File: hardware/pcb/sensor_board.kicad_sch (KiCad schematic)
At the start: 43 parts, among them J1 12V_INN, J10 CHT2 Termopar, J11 CHT3 Termopar, J12 CHT4 Termopar, J15 GPS NEO-6M, J2 Olje Temp NTC, J3 IAT Inntaksluft NTC, J4 Olje Trykk 0-10bar, J5 Lambda Innovate LC-2, J6 Batteri 12-15V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

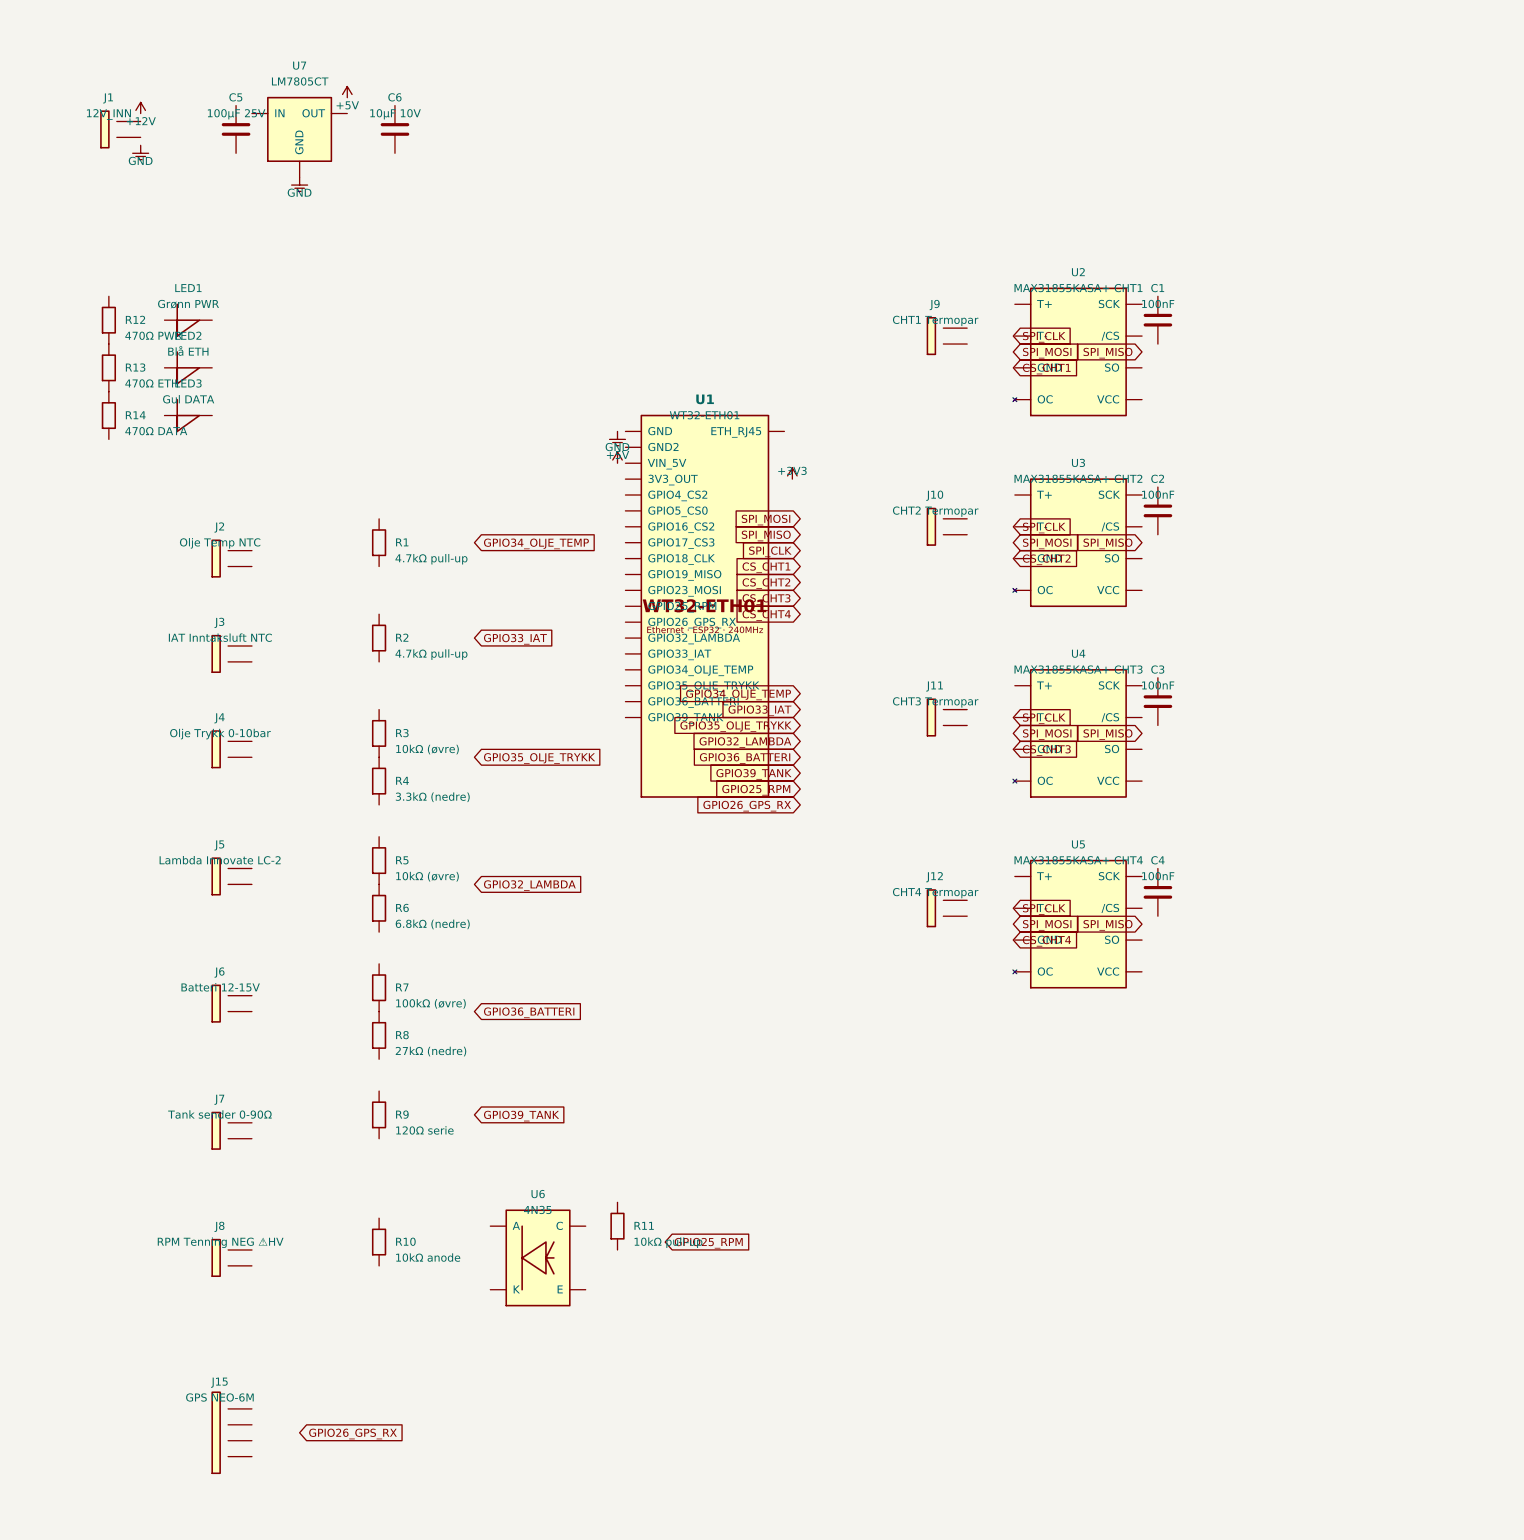
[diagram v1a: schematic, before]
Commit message: Sensorkortet v2: GPIO-fix, EGT1, vifte-MOSFET, GPS fjernet
- Rettede GPIO-pinner (ETH-konflikt): SCK=GPIO14, MISO=GPIO12
  CS: CHT1=GPIO5, CHT2=GPIO13, CHT3=GPIO15, CHT4=GPIO17
  RPM=GPIO4, EGT1=GPIO16, FAN=GPIO2
- Lagt til U8 (MAX31855 for EGT1 eksostemperatur)
- Lagt til Q1 (IRLB8721 MOSFET) for 12V viftestyring
- Lagt til D1 (1N4007 flyback-diode) for motorbeskyttelse
- Lagt til R15 (100R gate), R16 (10k pull-down), J17 (vifte-klemme)
- Fjernet GPS-header (NEO-6M kobles direkte til RPi via USB)
- 291 gyldige UUIDs, 0 duplikater, 0 ugyldige pin-shapes

https://claude.ai/code/session_01NVvsy3kMr9piDWfs5WdvpG
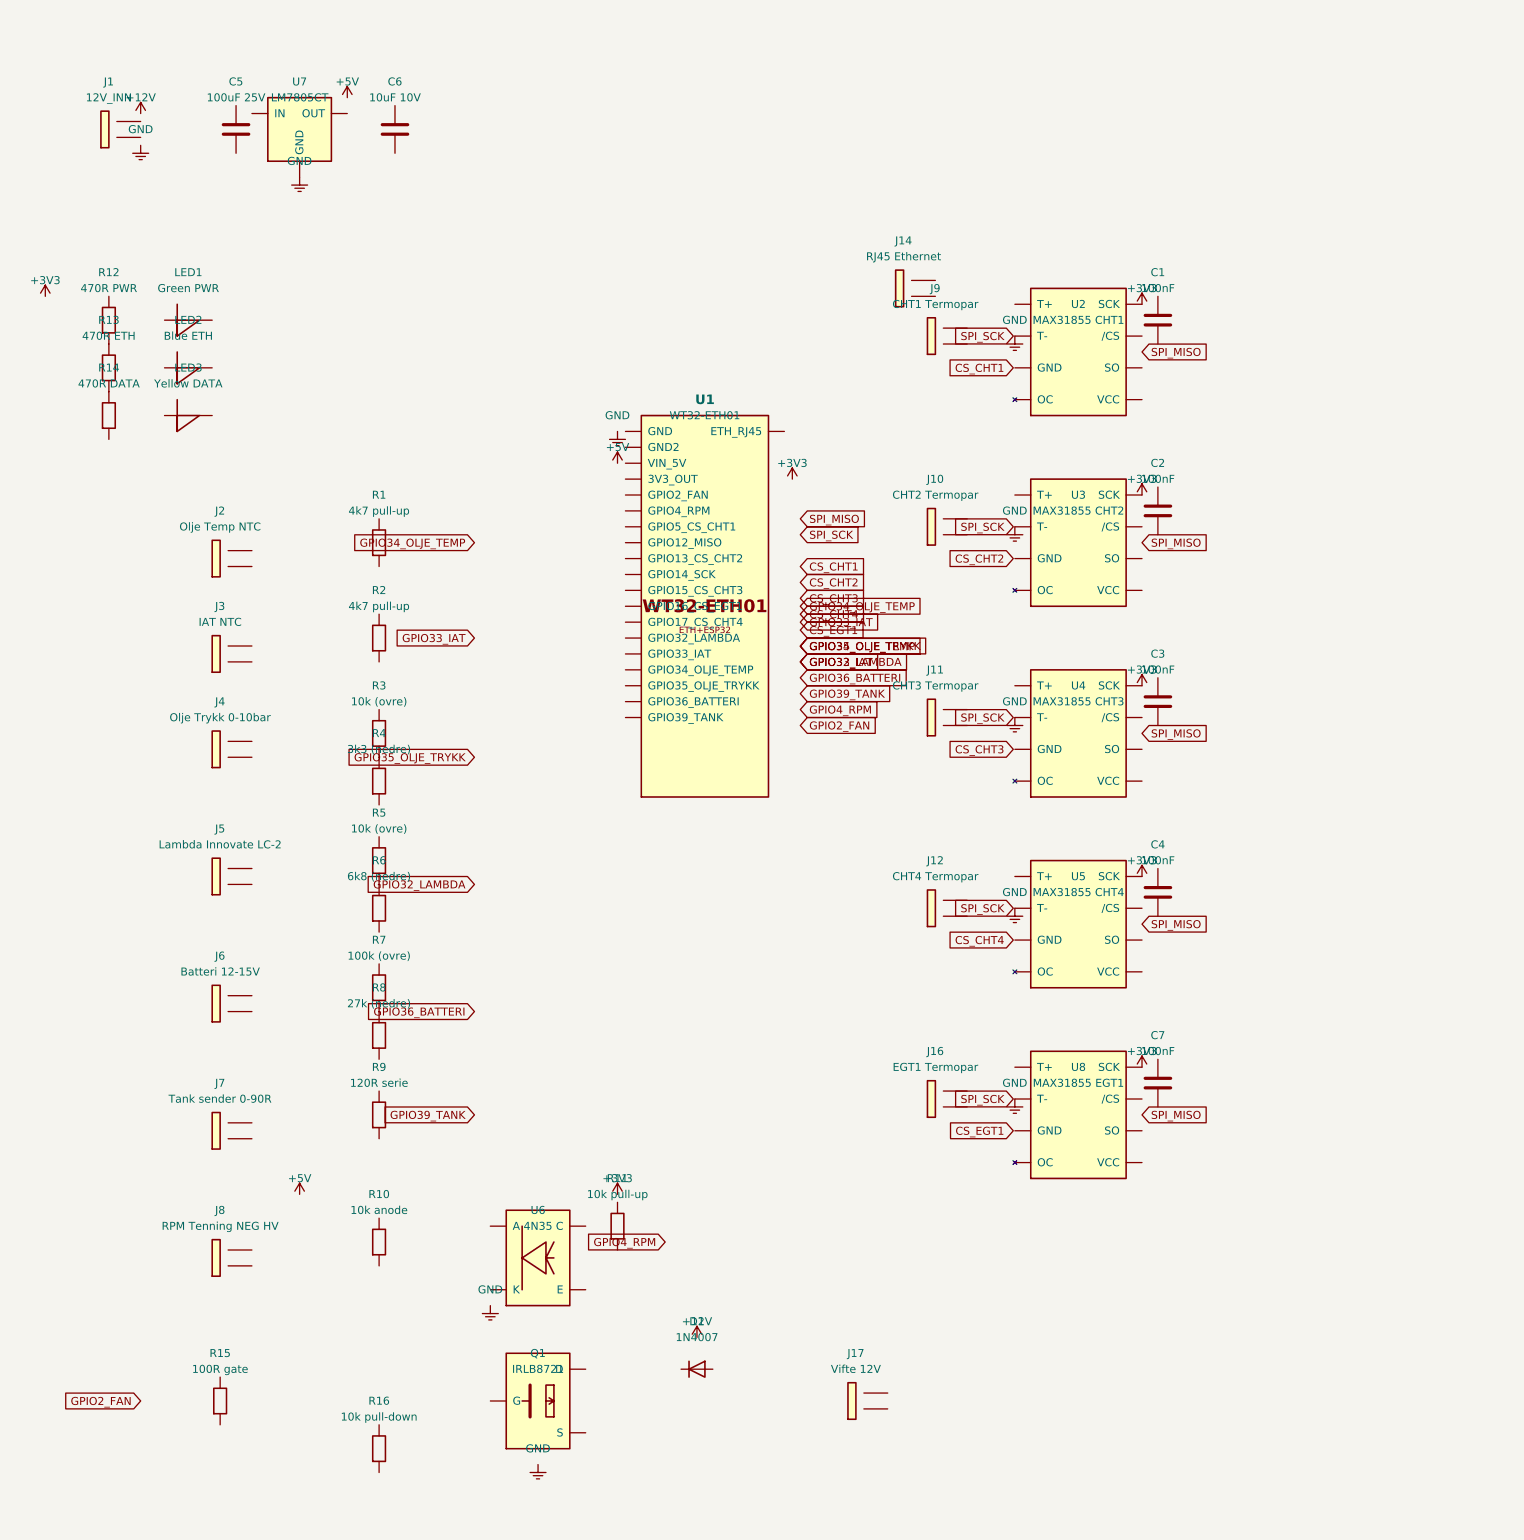
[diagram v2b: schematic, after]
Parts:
- removed J15: GPS NEO-6M, Connector_PinHeader_2.54mm:PinHeader_1x04_P2.54mm_Vertical, symbol Connector:Conn_01x04
- added C7: 100nF, Capacitor_SMD:C_0402_1005Metric, symbol Device:C
- added D1: 1N4007, Diode_THT:D_DO-41_SOD81_P10.16mm_Horizontal, symbol Device:D
- added J14: RJ45 Ethernet, Connector_RJ:RJ45_Amphenol_RJHSE538X_Horizontal, symbol Connector:Conn_01x02
- added J16: EGT1 Termopar, TerminalBlock:TerminalBlock_Altech_AK300-2_P3.50mm, symbol Connector:Conn_01x02
- added J17: Vifte 12V, TerminalBlock_Phoenix:TerminalBlock_Phoenix_MKDS-1,5-2_1x02_P5.00mm_Horizontal, symbol Connector:Conn_01x02
- added Q1: IRLB8721, Package_TO_SOT_THT:TO-220-3_Vertical, symbol IRLB8721
- added R15: 100R gate, Resistor_SMD:R_0402_1005Metric, symbol Device:R
- added R16: 10k pull-down, Resistor_SMD:R_0402_1005Metric, symbol Device:R
- added U8: MAX31855 EGT1, Package_SO:SOIC-8_3.9x4.9mm_P1.27mm, symbol MAX31855
- C5: value 100µF 25V -> 100uF 25V
- C6: value 10µF 10V -> 10uF 10V
- J3: value IAT Inntaksluft NTC -> IAT NTC
- J7: value Tank sender 0-90Ω -> Tank sender 0-90R
- J8: value RPM Tenning NEG ⚠HV -> RPM Tenning NEG HV
- LED1: value Grønn PWR -> Green PWR
- LED2: value Blå ETH -> Blue ETH
- LED3: value Gul DATA -> Yellow DATA
- R1, R2: value 4.7kΩ pull-up -> 4k7 pull-up
- R10: value 10kΩ anode -> 10k anode
- R11: value 10kΩ pull-up -> 10k pull-up
- R12: value 470Ω PWR -> 470R PWR
- R13: value 470Ω ETH -> 470R ETH
- R14: value 470Ω DATA -> 470R DATA
- R3, R5: value 10kΩ (øvre) -> 10k (ovre)
- R4: value 3.3kΩ (nedre) -> 3k3 (nedre)
- R6: value 6.8kΩ (nedre) -> 6k8 (nedre)
- R7: value 100kΩ (øvre) -> 100k (ovre)
- R8: value 27kΩ (nedre) -> 27k (nedre)
- R9: value 120Ω serie -> 120R serie
- U1: LCSC Module - kjøpes separat -> Module - separat
- U2: value MAX31855KASA+ CHT1 -> MAX31855 CHT1
- U3: value MAX31855KASA+ CHT2 -> MAX31855 CHT2
- U4: value MAX31855KASA+ CHT3 -> MAX31855 CHT3
- U5: value MAX31855KASA+ CHT4 -> MAX31855 CHT4
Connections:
- net +3V3: now also U2.4 (SCK), U3.4 (SCK), U4.4 (SCK), U5.4 (SCK), U8.4 (SCK)
- net GND: now also U2.2 (T-), U3.2 (T-), U4.2 (T-), U5.2 (T-), U8.2 (T-)
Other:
- title: VW Boble 1956 — Sensor Interface Board -> VW Boble 1956 — Sensor Interface Board v2

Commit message: Sensorkortet v3: redesign med pinner pa begge sider og nummererte klemmer
- WT32-ETH01 symbol: analoge pinner til VENSTRE, SPI-pinner til HOYRE
- Sensorer plassert pa venstre side med tydelig nummerering 1-13
- MAX31855 (CHT1-4 + EGT1) plassert pa hoyre side
- Kabelliste-legend pa skjema (1=Lambda, 2=IAT... 13=EGT1)
- A2 papirstorrelse for bedre lesbarhet
- 342 gyldige UUIDs, 0 feil

https://claude.ai/code/session_01NVvsy3kMr9piDWfs5WdvpG
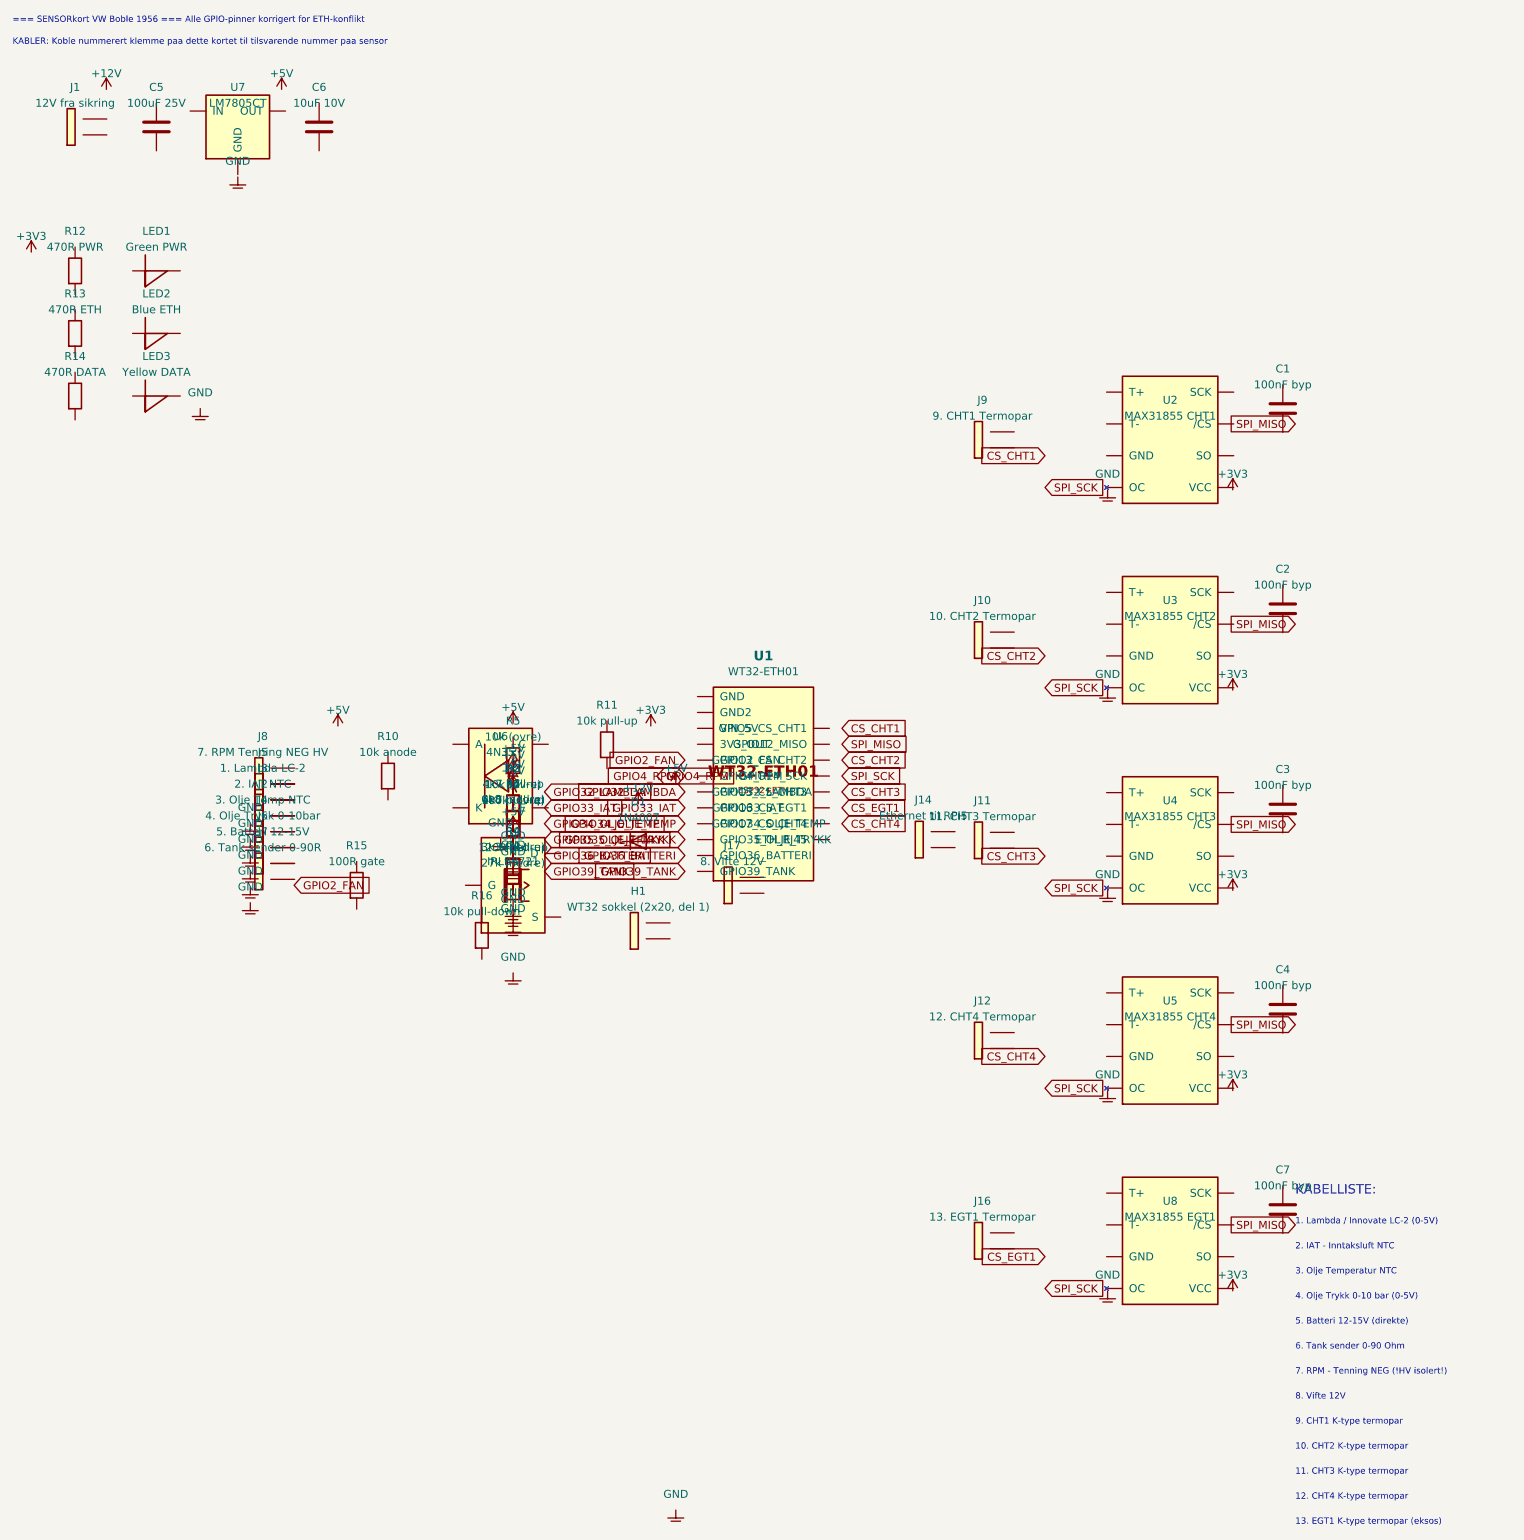
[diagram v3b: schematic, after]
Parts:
- added H1: WT32 sokkel (2x20, del 1), Connector_PinHeader_2.54mm:PinHeader_2x20_P2.54mm_Vertical, symbol Connector:Conn_01x02
- C1, C2, C3, C4, C7: value 100nF -> 100nF byp
- J1: value 12V_INN -> 12V fra sikring
- J10: value CHT2 Termopar -> 10. CHT2 Termopar
- J11: value CHT3 Termopar -> 11. CHT3 Termopar
- J12: value CHT4 Termopar -> 12. CHT4 Termopar
- J14: value RJ45 Ethernet -> Ethernet til RPi5
- J16: value EGT1 Termopar -> 13. EGT1 Termopar
- J17: value Vifte 12V -> 8. Vifte 12V
- J2: value Olje Temp NTC -> 3. Olje Temp NTC
- J3: value IAT NTC -> 2. IAT NTC
- J4: value Olje Trykk 0-10bar -> 4. Olje Trykk 0-10bar
- J5: value Lambda Innovate LC-2 -> 1. Lambda LC-2
- J6: value Batteri 12-15V -> 5. Batteri 12-15V
- J7: value Tank sender 0-90R -> 6. Tank sender 0-90R
- J8: value RPM Tenning NEG HV -> 7. RPM Tenning NEG HV
- J9: value CHT1 Termopar -> 9. CHT1 Termopar
- R9: value 120R serie -> 120R pull-up
- U1: LCSC Module - separat -> Bestilles separat
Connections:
- net +3V3: no longer U2.4 (SCK), U3.4 (SCK), U4.4 (SCK), U5.4 (SCK), U8.4 (SCK)
- net GND: no longer U2.2 (T-), U3.2 (T-), U4.2 (T-), U5.2 (T-), U7.2 (GND), U8.2 (T-)
- net at R14.1: no longer R13.2
- net at J6.1 (Pin_1): now also J4.2 (Pin_2)
- net at J6.2 (Pin_2): now also J7.1 (Pin_1)
- net at J3.1 (Pin_1): now also J5.2 (Pin_2)
- net at J3.2 (Pin_2): now also J2.1 (Pin_1)
- net at R4.1: now also R6.2; no longer R3.2
- net at J5.1 (Pin_1): now also J8.2 (Pin_2)
- net at J4.1 (Pin_1): now also J2.2 (Pin_2)
- net at R13.1: no longer R12.2
- net at R1.2: now also R9.1
- net at R8.1: no longer R7.2
- net at R6.1: no longer R5.2
- net at R3.1: now also R5.2
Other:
- note added: "1. Lambda / Innovate LC-2 (0-5V)"
- note added: "10. CHT2 K-type termopar"
- note added: "11. CHT3 K-type termopar"
- note added: "12. CHT4 K-type termopar"
- note added: "13. EGT1 K-type termopar (eksos)"
- note added: "2. IAT - Inntaksluft NTC"
- note added: "3. Olje Temperatur NTC"
- note added: "4. Olje Trykk 0-10 bar (0-5V)"
- note added: "5. Batteri 12-15V (direkte)"
- note added: "6. Tank sender 0-90 Ohm"
- note added: "7. RPM - Tenning NEG (!HV isolert!)"
- note added: "8. Vifte 12V"
- note added: "9. CHT1 K-type termopar"
- note added: "=== SENSORkort VW Boble 1956 === Alle GPIO-pinner korrigert for ETH-konflikt"
- note added: "KABELLISTE:"
- note added: "KABLER: Koble nummerert klemme paa dette kortet til tilsvarende nummer paa sensor"
- title: VW Boble 1956 — Sensor Interface Board v2 -> VW Boble 1956 - Sensor Interface Board v3

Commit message: Redesign sensor board: Teensy 4.1, password gate, updated HW panel
- Teensy 4.1 + WIZ820io Ethernet replaces WT32-ETH01/ESP32
- MP2307DN 3A buck converter (~90% efficiency)
- Full KiCad 7 schematic with 22 components, dot-to-dot net numbering (1–58)
- Wired SVG schematic v0.2 with proper IEC symbols
- BOM + PCBWay design brief
- HW panel: 5 tabs (overview, connectors, BOM, schematic, firmware)
- Password gate (1337) protecting the site
- Generic J0–J30 connector naming for universal use
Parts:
- U1: footprint Module:WT32-ETH01 -> WT32-ETH01:WT32-ETH01_Socket_2x20
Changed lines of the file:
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@@
   (property "Reference" "U1" (at 130.0 109.53 0) (effects (font (size 1.524 1.524) (bold yes))))
   (property "Value" "WT32-ETH01" (at 130.0 112.03 0) (effects (font (size 1.27 1.27))))
-  (property "Footprint" "Module:WT32-ETH01" (at 0 0 0) (effects (font (size 1.27 1.27)) (hide yes)))
+  (property "Footprint" "WT32-ETH01:WT32-ETH01_Socket_2x20" (at 0 0 0) (effects (font (size 1.27 1.27)) (hide yes)))
   (property "LCSC" "Bestilles separat" (at 0 0 0) (effects (font (size 1.27 1.27)) (hide yes)))
   (pin "1")
